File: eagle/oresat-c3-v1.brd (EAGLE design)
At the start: 99.8 x 94.7 mm, 173 parts, among them J1 J-SAMTEC-TFM-110-X1-XXX-D-RA, J12 U.FL, J13 U.FL, J14 U.FL, J15 HARWIN-2X8X1.27, J16 U.FL, J17 U.FL, J18 U.FL, J19 HARWIN-2X8X1.27, J2 U.FL, J3 U.FL, J4 U.FL, J6 J-SAMTEC-TFM-120-X1-XXX-D-RA, J7 FTSH-105-XX-X-DV-K, Q1 MOSFET-PCH-SOT23-6, U1 MAX892LEUA+T21-0036K-L, U11 U-ONSEMI-AX5043, U12 LP2985XX-N, U13 U-ONSEMI-AX5043, U14 LP2985XX-N, U2 TCAN330, U3 TCAN330, U4 TPS259621 - eFuse, U5 TPS62111RSA, U6 MAX6374KA-T21-0078H-L, U7 STM32F446RE, U8 SFEM016GB1EM1TO-A-HG-111-STD, X1 16MHZ-2.5x2mm, X3 TAITIEN-TY, X4 TAITIEN-TY

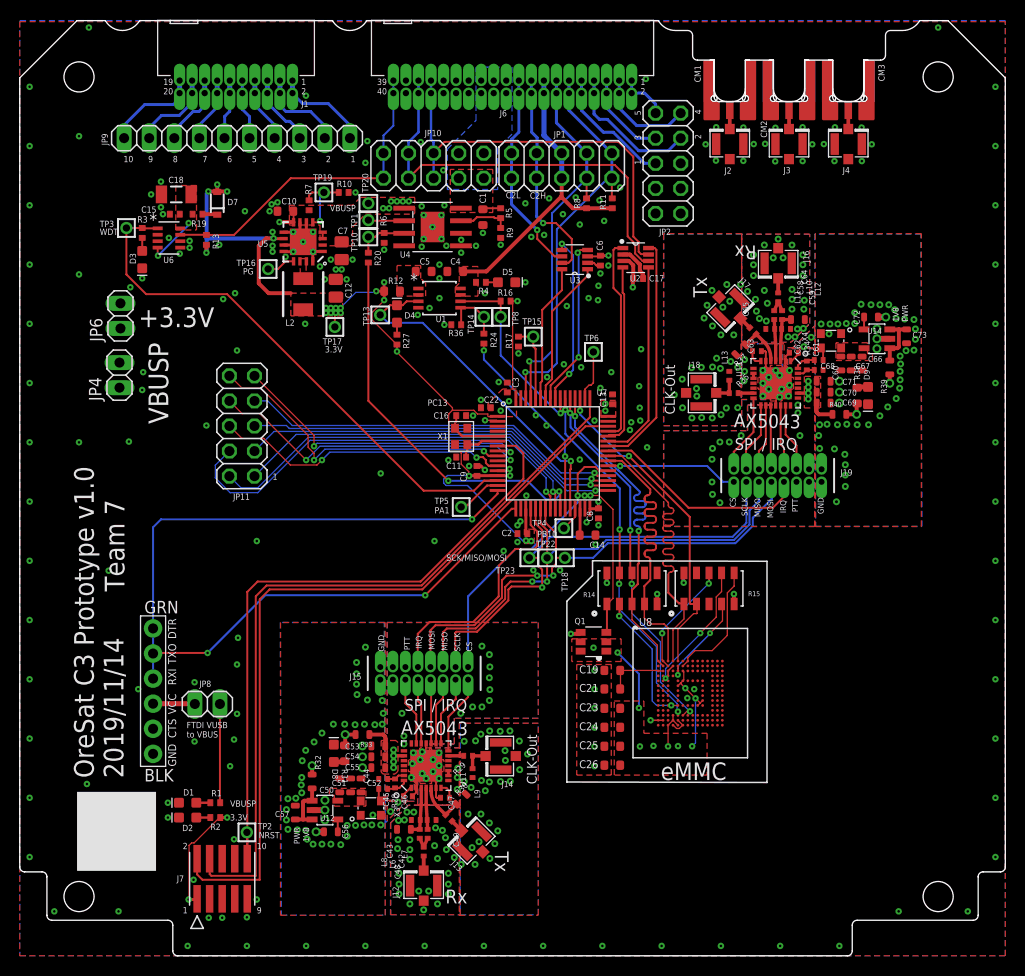
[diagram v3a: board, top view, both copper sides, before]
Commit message: Ran an initial ERC DRC on the v1 board, cleared some errors and left the rest for a board review
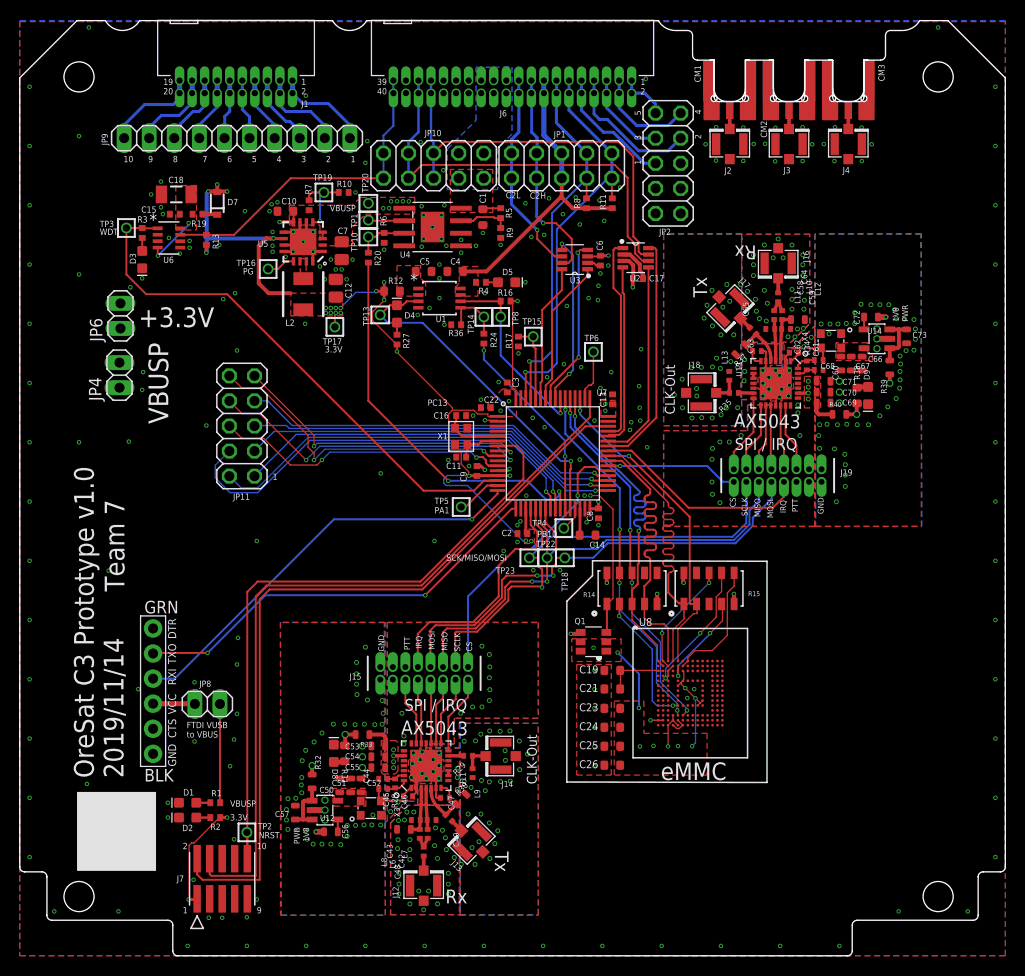
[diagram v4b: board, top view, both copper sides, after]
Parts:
- turned R35 to 0 degrees
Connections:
- removed net REF-OUT1: J14.FEED, R29.2, R30.1
- removed net REF-OUT2: J18.FEED, R35.2, R37.1
- net SYSCLK1: now also J14.FEED, R29.2, R30.1
- net SYSCLK2: now also J18.FEED, R35.2, R37.1
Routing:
- net USART2_TX: track 52.0 -> 43.0 mm
- net SYSCLK2: track 1.22 -> 4.15 mm
- net REF-OUT1: track 2.64 -> 0.00 mm
- net REF-OUT2: track 2.64 -> 0.00 mm
- net SYSCLK1: track 1.23 -> 3.85 mm
- net SDIO_D0: track 32.7 -> 32.0 mm
- net SDIO_CK: track 37.8 -> 37.3 mm

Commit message: implemented changes after design Review with Andrew
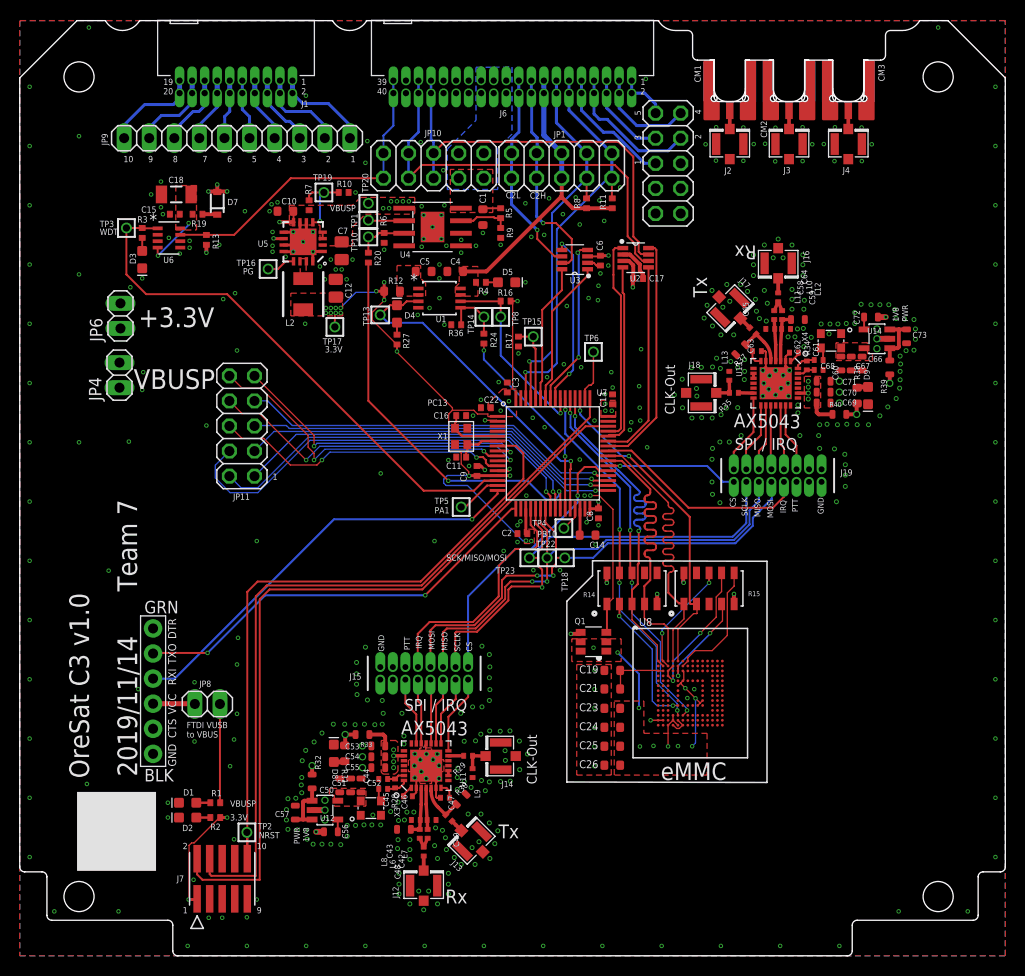
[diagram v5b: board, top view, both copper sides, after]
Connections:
- removed net GNDR: C43.1, C44.2, C46.2, C47.1, C50.2, C51.2, C52.2, C53.2, C54.2, C55.2, C56.2, C57.2, C59.1, C60.2, C62.2, C63.1, C66.2, C67.2, C68.2, C69.2, C70.2, C71.2, C72.2, C73.2, D8.C, D9.C, J15.15, J19.15, L11.1, L12.2, L13.1, L7.1, L8.2, L9.1, R30.2, R37.2, U11.2, U11.6, U11.PAD, U12.2, U13.2, U13.6, U13.PAD, U14.2, X3.2, X4.2
- net GND: now also C43.1, C44.2, C46.2, C47.1, C50.2, C51.2, C52.2, C53.2, C54.2, C55.2, C56.2, C57.2, C59.1, C60.2, C62.2, C63.1, C66.2, C67.2, C68.2, C69.2, C70.2, C71.2, C72.2, C73.2, D8.C, D9.C, J15.15, J19.15, L11.1, L12.2, L13.1, L7.1, L8.2, L9.1, R30.2, R37.2, U11.2, U11.6, U11.PAD, U12.2, U13.2, U13.6, U13.PAD, U14.2, X3.2, X4.2
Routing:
- net 3.3V: track 376.2 -> 120.0 mm, vias 48 -> 49
- net GNDR: track 13.5 -> 0.00 mm, vias 262 -> 0
- net GND: track 25.3 -> 38.7 mm, vias 218 -> 480
- removed copper zone on layer 1, net GNDR
- removed copper zone on layer 15, net GNDR
- removed copper zone on layer 16, net GNDR
- removed copper zone on layer 2, net GNDR
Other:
- board text added: "OreSat C3 v1.0"
- board text removed: "OreSat C3 Prototype v1.0"

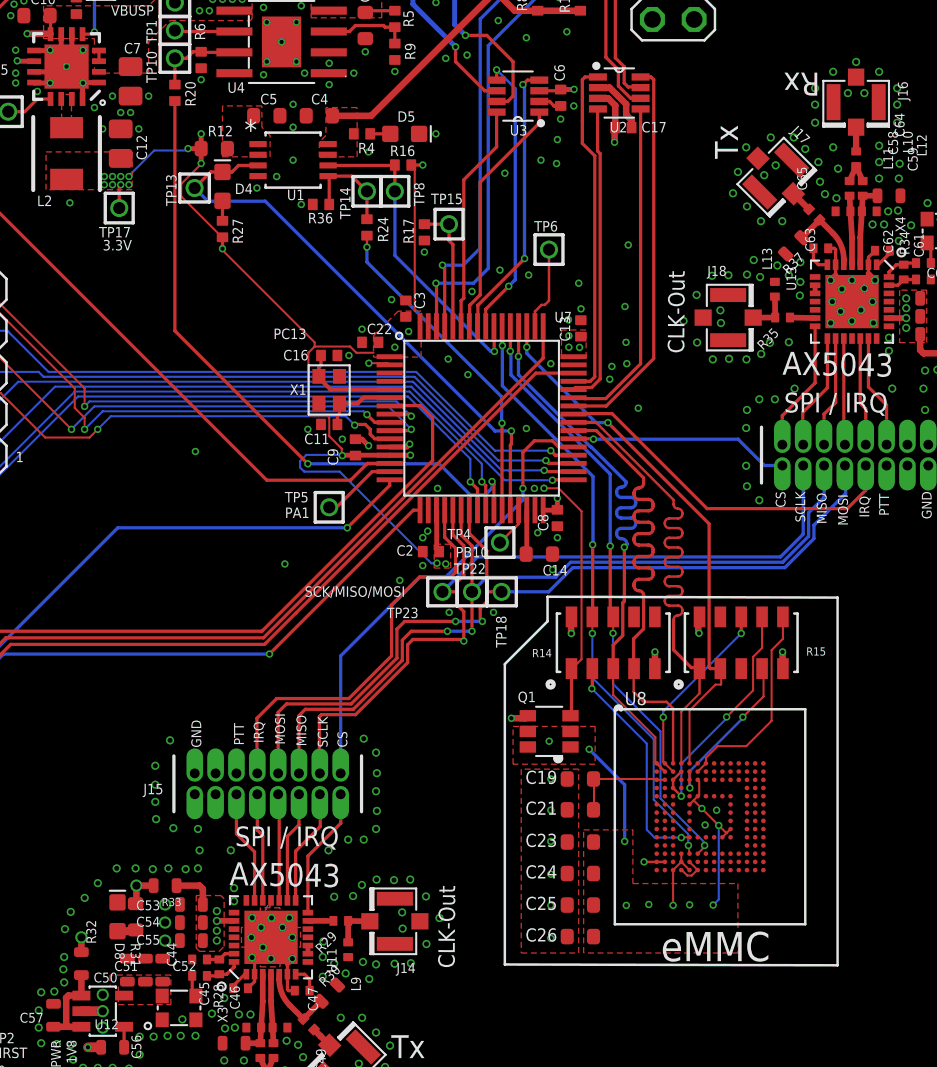
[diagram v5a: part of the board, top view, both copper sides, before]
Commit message: Cleared errors for eMMC Added documentation for eMMC
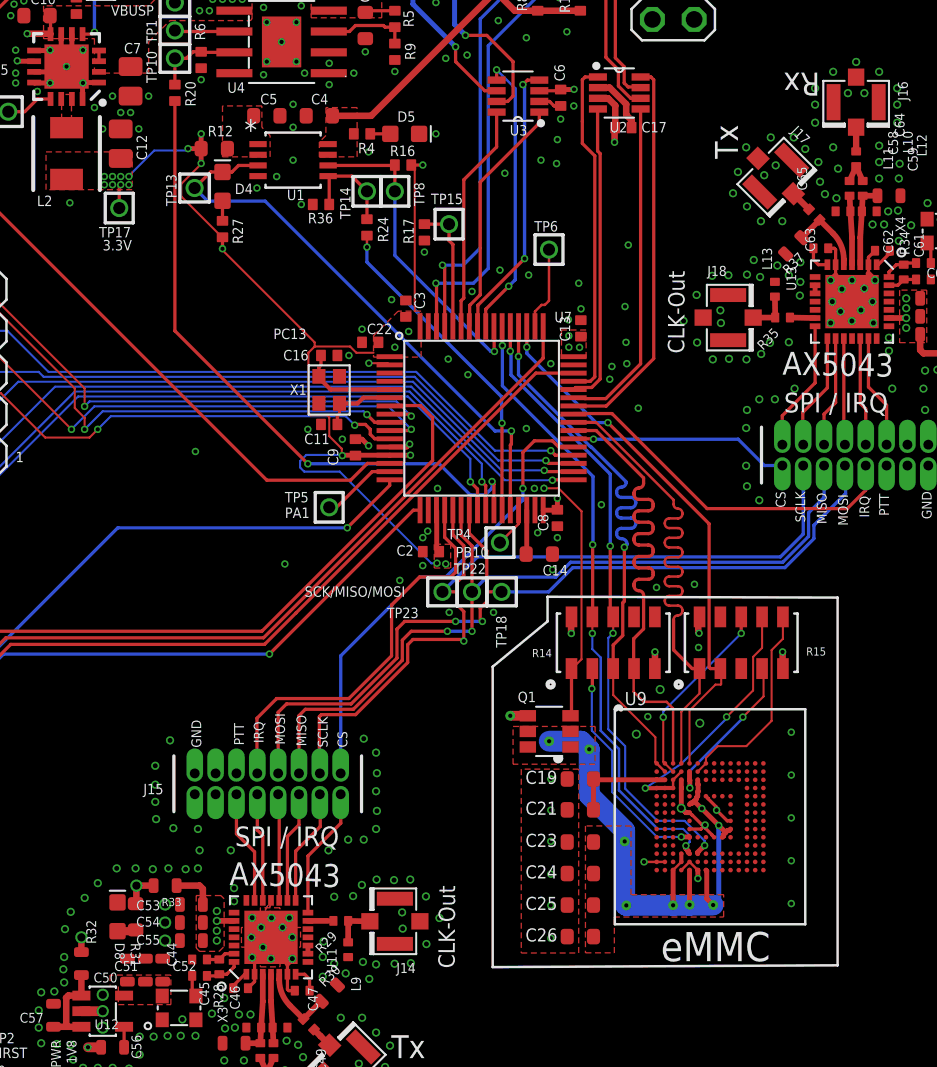
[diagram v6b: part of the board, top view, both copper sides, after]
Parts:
- removed U8: SFEM016GB1EM1TO-A-HG-111-STD, U-Generic-eMMC-153pin:BGA-153(11.5X13)(EMMC-BA)
- added U9: SFEM016GB1EM1TO-A-HG-111-STD, U-C3-eMMC-153pin:BGA-153(11.5X13)(EMMC-BA)
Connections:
- net GND: now also U9.A6, U9.C4, U9.D4, U9.E7, U9.G5, U9.H10, U9.J5, U9.K8, U9.N1, U9.N2, U9.N5, U9.P4, U9.P6; no longer U8.A6, U8.C4, U8.E7, U8.G5, U8.H10, U8.J5, U8.K8, U8.N1, U8.N2, U8.N5, U8.P4, U8.P6
- net MMC_VDD: now also U9.C6, U9.E6, U9.F5, U9.J10, U9.K9, U9.M4, U9.N4, U9.P3, U9.P5, U9.P7; no longer U8.C6, U8.E6, U8.F5, U8.J10, U8.K9, U8.M4, U8.N4, U8.P3, U8.P5, U8.P7
- net SDIO_CK: now also U9.M6; no longer U8.M6
- net SDIO_CMD: now also U9.M5; no longer U8.M5
- net SDIO_D0: now also U9.A3; no longer U8.A3
- net SDIO_D1: now also U9.A4; no longer U8.A4
- net SDIO_D2: now also U9.A5; no longer U8.A5
- net SDIO_D3: now also U9.A1, U9.B2; no longer U8.A1, U8.B2
- net SDIO_D4: now also U9.A2, U9.B3; no longer U8.A2, U8.B3
- net SDIO_D5: now also U9.B4, U9.C3, U9.D1, U9.D2, U9.D3; no longer U8.B4, U8.C3, U8.D3
- net SDIO_D6: now also U9.B5, U9.C5; no longer U8.B5, U8.C5
- net SDIO_D7: now also U9.A7, U9.B6; no longer U8.A7, U8.B6
- net SDIO_RST: now also U9.K5; no longer U8.K5
- net VDDI: now also U9.C1, U9.C2; no longer U8.C2
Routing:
- net MMC_VDD: track 20.9 -> 36.4 mm
- net GND: track 38.7 -> 46.6 mm, vias 480 -> 493
- net SDIO_D5: track 14.9 -> 16.5 mm
- net SDIO_CK: track 37.3 -> 38.5 mm
- net SDIO_CMD: track 36.9 -> 38.0 mm
- removed copper zone on layer 15, net MMC_VDD

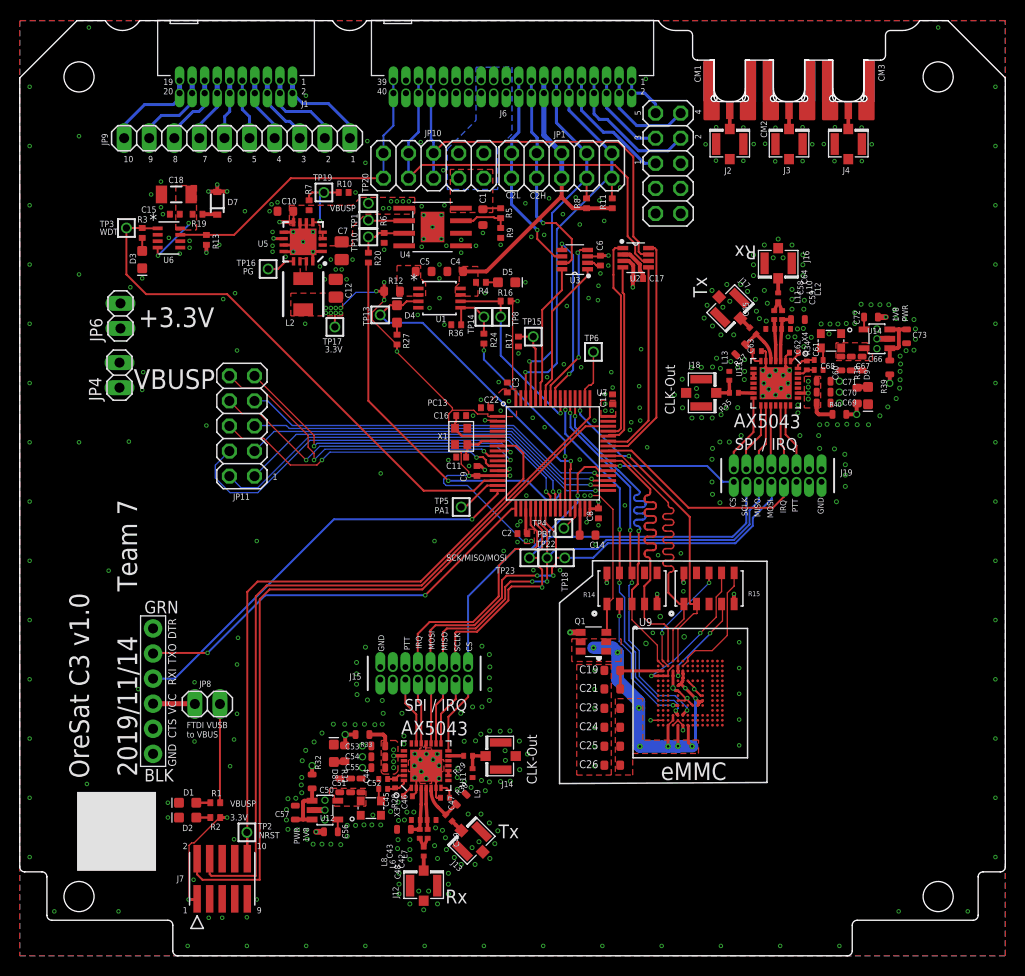
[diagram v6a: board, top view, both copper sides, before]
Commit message: Made Design review changes to C3 board
updated changes made in design review doc
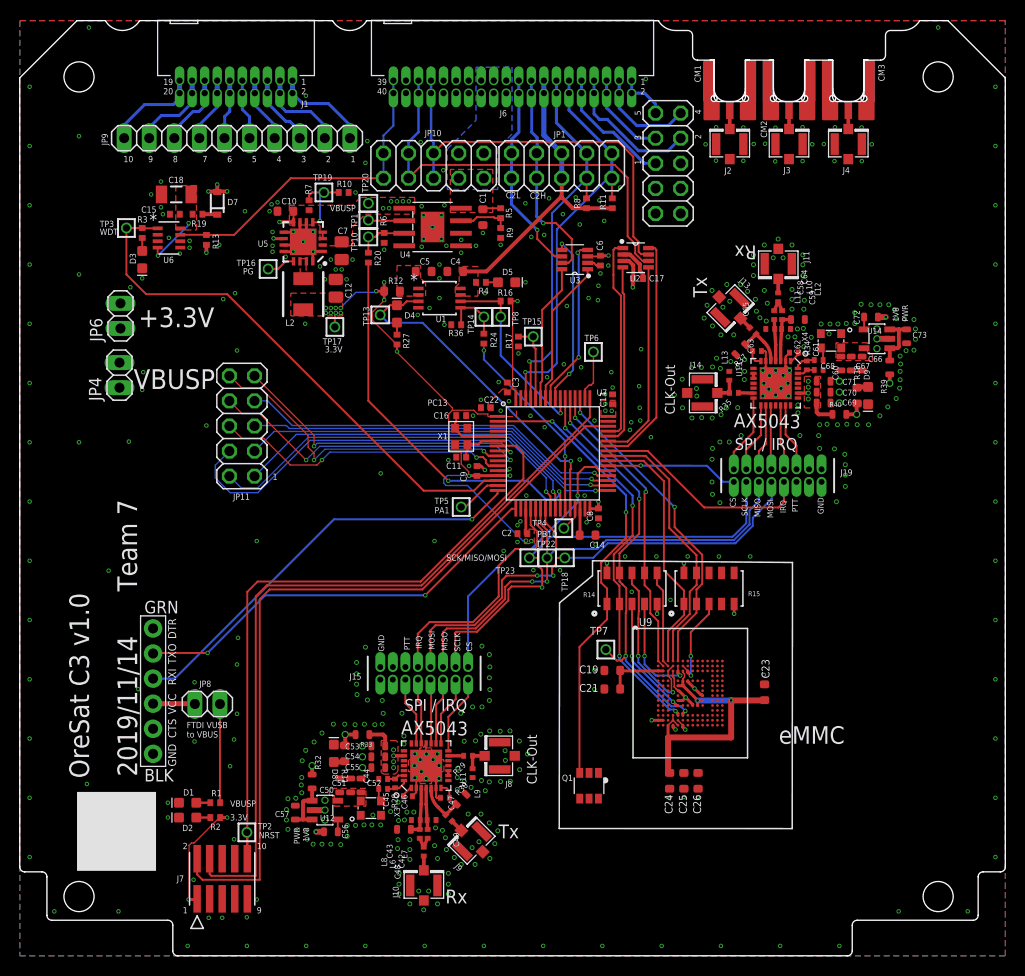
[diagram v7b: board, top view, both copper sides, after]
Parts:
- removed J12, J16, J17, J18: U.FL, SparkFun-Connectors:U.FL
- added J10, J11, J8, J9: U.FL, SparkFun-Connectors:U.FL
- added TP7: TEST-POINT, Tova:2MM-TEST-POINT
- moved J13 60.0 mm to (71.9, 65.6), turned to 315 degrees
- moved J14 42.1 mm to (69.1, 57.0), turned to 0 degrees
- moved C23 15.5 mm to (75.4, 26.7), turned to 90 degrees
- moved Q1 14.6 mm to (57.6, 17.2), turned to 180 degrees
- moved C26 8.83 mm to (68.7, 17.7), turned to 270 degrees
- moved C25 8.05 mm to (67.2, 17.7), turned to 270 degrees
- moved C24 7.95 mm to (65.8, 17.7), turned to 270 degrees
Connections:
- removed net RX2: C64.1, J16.FEED
- new net N$2: C64.1, J11.FEED
- new net N$4: R14.6
- net GND: now also J10.1, J10.2, J11.1, J11.2, J13.1, J13.2, J14.1, J14.2, J15.13, J15.14, J15.16, J19.13, J19.14, J19.16, J8.1, J8.2, J9.1, J9.2
- net MMC_VDD: no longer U9.P7
- net RX1: now also J10.FEED; no longer J12.FEED
- net SDIO_CK: now also R14.9, TP7.1; no longer R14.8
- net SDIO_CMD: now also R14.2; no longer R14.9
- net SDIO_D0: now also R15.1; no longer R14.4
- net SDIO_D1: now also R15.9; no longer R15.1
- net SDIO_D3: now also R14.7; no longer R14.3
- net SDIO_D4: no longer R15.8
- net SDIO_D5: now also R14.8; no longer R15.7, U9.D1, U9.D2
- net SDIO_D6: now also R14.4; no longer R15.4
- net SDIO_D7: now also R15.3, U9.C7; no longer R15.6, U9.A7
- net SDIO_RST: now also R14.3; no longer R14.2
- net SYSCLK1: now also J8.FEED; no longer J14.FEED
- net SYSCLK2: now also J14.FEED; no longer J18.FEED
- net TX1: now also J9.FEED; no longer J13.FEED
- net TX2: now also J13.FEED; no longer J17.FEED
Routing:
- net MMC_PWR: track 30.8 -> 46.7 mm
- net MMC_VDD: track 36.4 -> 29.1 mm, vias 9 -> 2
- net SDIO_D0: track 32.0 -> 26.2 mm
- net SDIO_D1: track 33.5 -> 27.7 mm
- net SDIO_D3: track 35.3 -> 30.9 mm
- net SDIO_CK: track 38.5 -> 42.0 mm
- net SDIO_D7: track 12.6 -> 9.32 mm, vias 0 -> 2
- net 3.3V: track 120.0 -> 118.1 mm, vias 49 -> 48
- net SDIO_D4: track 11.6 -> 9.88 mm, vias 2 -> 0
- net SDIO_RST: track 13.9 -> 12.3 mm
- net RX2: track 1.48 -> 0.00 mm
- net N$2: track 0.00 -> 1.43 mm
- net SDIO_D6: track 10.2 -> 11.2 mm
- net GND: track 46.6 -> 45.8 mm, vias 493 -> 488
- net SDIO_CMD: track 38.0 -> 38.7 mm
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- removed copper zone on layer 1, net MMC_VDD
